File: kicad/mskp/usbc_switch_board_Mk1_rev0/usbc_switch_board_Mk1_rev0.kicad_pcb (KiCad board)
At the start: 2 copper layers, 54.4 x 29 mm, 27 parts, among them J1 USB_C_Receptacle_USB2.0_14P, J2 USB_C_Receptacle_USB2.0_14P, J3 USB_A, J4 USB_out_pads, J5 Switch_ctrl_pads, Q1 2N3906, Q2 2N3904, U1 FSUSB42MUX, U2 AMS1117-3.3

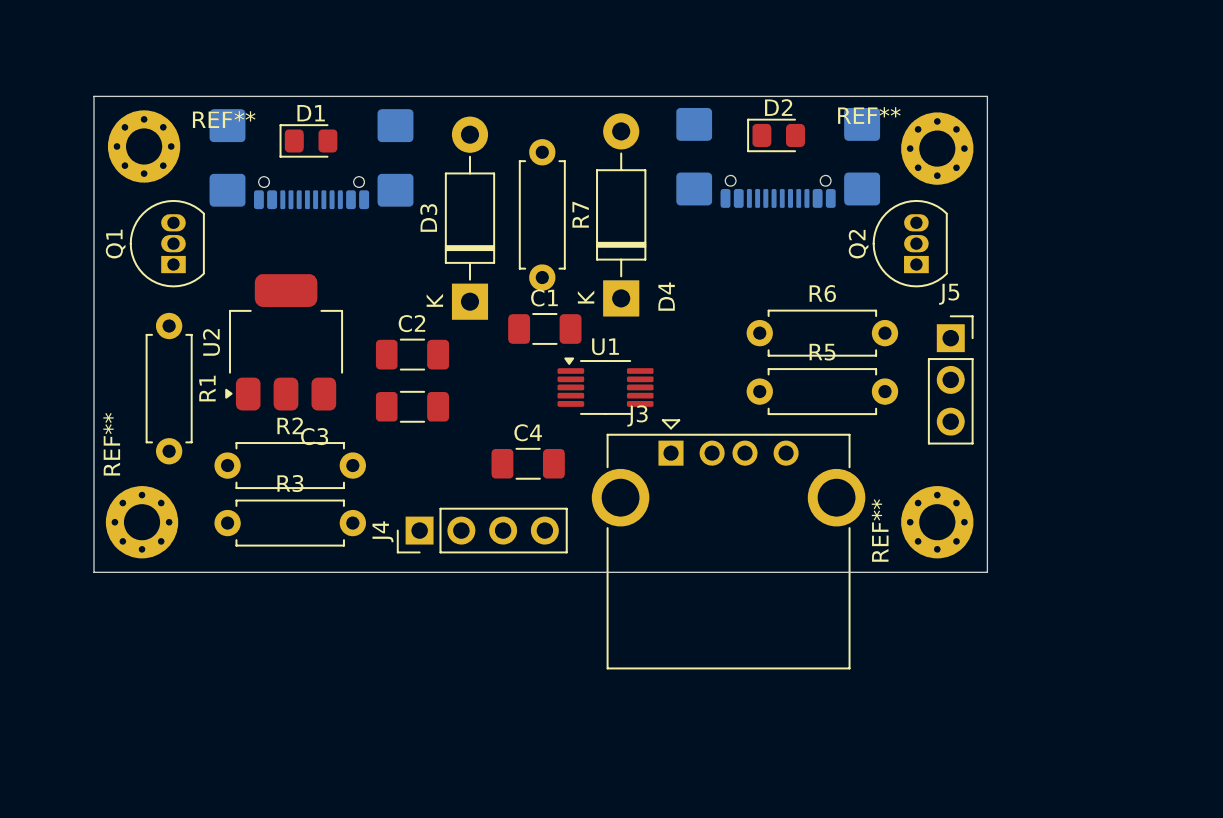
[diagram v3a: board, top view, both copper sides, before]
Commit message: Refines usb and mouse control boards with outline and GND
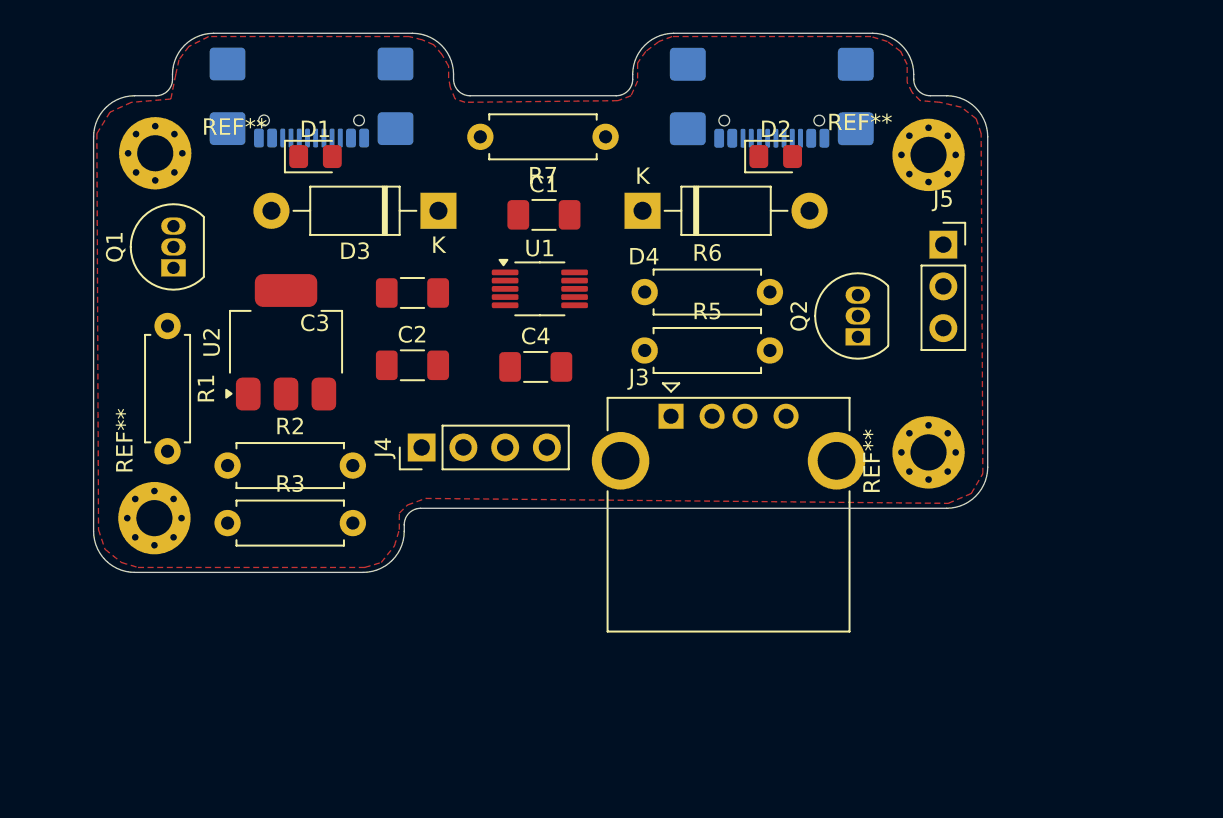
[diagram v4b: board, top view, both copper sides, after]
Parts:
- moved R5 7.43 mm to (136.6, 81.5)
- moved R6 7.43 mm to (136.6, 77.9)
- moved U1 7.21 mm to (130.2, 77.8)
- moved C1 6.94 mm to (130.5, 73.2)
- moved C3 6.92 mm to (122.5, 78.0)
- moved C4 5.91 mm to (130.0, 82.5)
- moved D3 5.85 mm to (124.1, 73.0), turned to 180 degrees
- moved J5 5.71 mm to (154.8, 75.1)
- moved Q2 5.66 mm to (149.6, 80.7)
- moved D4 5.49 mm to (136.5, 73.0), turned to 0 degrees
- moved J4 5.06 mm to (123.1, 87.4)
- moved REF** 4.28 mm to (153.9, 87.7)
- moved R7 3.96 mm to (134.2, 68.5), turned to 180 degrees
- moved J1 3.75 mm to (116.4, 64.9)
- moved J2 3.69 mm to (144.4, 64.9)
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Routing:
- added copper zone on F.Cu, net GND
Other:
- board size 54.4 x 29 mm -> 54.4 x 32.8 mm

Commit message: Initial PCB layout for usbc_switch_board_Mk1_rev0
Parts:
- moved D1 2.11 mm to (116.4, 67.6)
- moved D2 2.11 mm to (144.4, 67.6)
- moved C1 0.20 mm to (130.5, 73.0)
- moved D4 0.13 mm to (136.6, 73.0)
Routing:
- net Net-(U1-VCC): track 0.00 -> 58.2 mm, vias 0 -> 6
- net /5V: track 0.00 -> 58.1 mm, vias 0 -> 1
- net /SEL: track 0.00 -> 54.0 mm
- net Net-(Q1-B): track 0.00 -> 53.7 mm, vias 0 -> 4
- net Net-(Q1-E): track 0.00 -> 53.2 mm, vias 0 -> 1
- net /D+: track 0.00 -> 33.6 mm, vias 0 -> 4
- net Net-(U1-HSD1-): track 0.00 -> 33.1 mm, vias 0 -> 4
- net Net-(U1-HSD1+): track 0.00 -> 31.7 mm, vias 0 -> 3
- net GND: track 0.00 -> 31.5 mm, vias 0 -> 4
- net /D-: track 0.00 -> 30.8 mm, vias 0 -> 4
- net Net-(U1-HSD2-): track 0.00 -> 25.4 mm, vias 0 -> 3
- net Net-(U1-HSD2+): track 0.00 -> 24.8 mm, vias 0 -> 4
- net Net-(U1-SEL): track 0.00 -> 17.6 mm
- net Net-(D2-A): track 0.00 -> 17.1 mm
- net Net-(J5-Pin_3): track 0.00 -> 15.4 mm
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
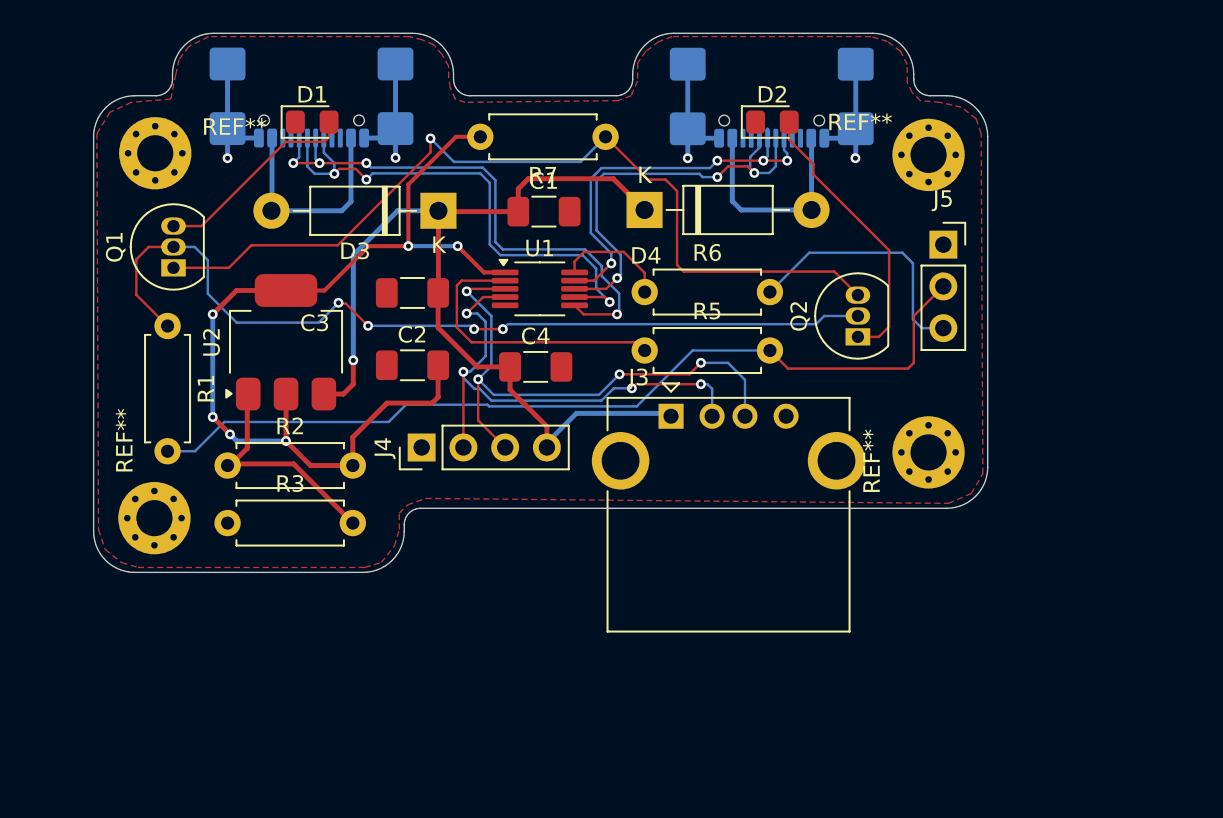
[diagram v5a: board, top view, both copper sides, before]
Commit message: Adds silkscreen to usbc_switch_board_Mk1_rev0 PCB
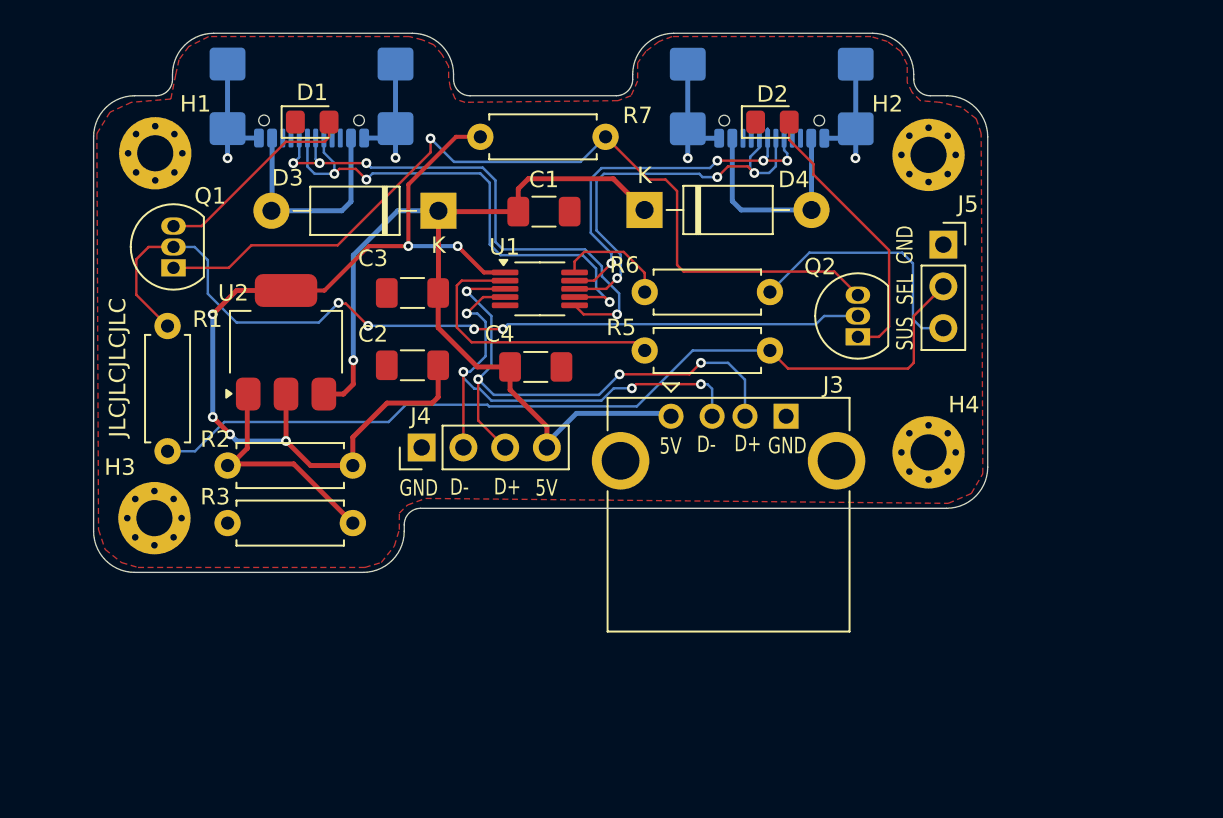
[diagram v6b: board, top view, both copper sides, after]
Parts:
- renumbered REF** to H1, REF** to H2, REF** to H3, REF** to H4
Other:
- board text added: "10-2024"
- board text added: "5V"
- board text added: "D+"
- board text added: "D-"
- board text added: "GND"
- board text added: "I"
- board text added: "Input"
- board text added: "JLCJLCJLCJLC"
- board text added: "MSKP-USB-C-SWITCH-MK.1-REV.0"
- board text added: "Mk"
- board text added: "Output 1"
- board text added: "Output 2"
- board text added: "SEL"
- board text added: "SUS"
- board text added: "USB-C Switch"
- board text added: "github.com/thegreatgramblinham"
